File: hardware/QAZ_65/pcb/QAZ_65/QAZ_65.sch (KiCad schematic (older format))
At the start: 97 parts, among them SW1 PTS525, U1 AP2112K-3.3, U2 STM32F042C6Tx, U3 LP5009RUKR, Y1 8.0000MHz

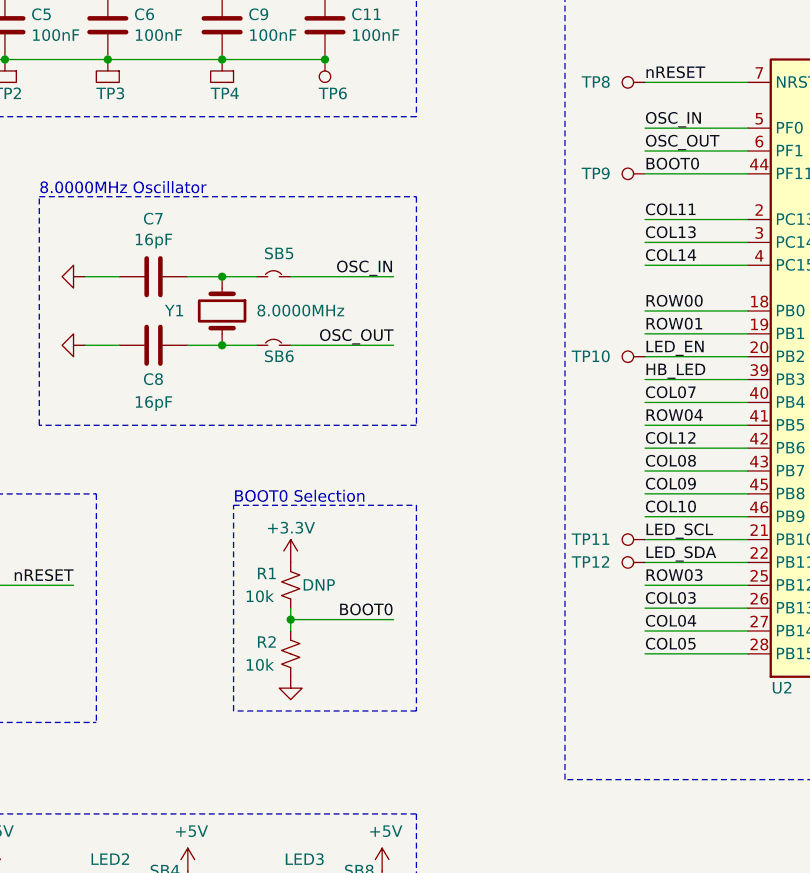
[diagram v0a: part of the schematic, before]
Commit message: qaz v1.1: fixes going from v1.0->v1.1
Changed from individual pull up/down on BOOT0 MCU pin to switch that can
easily change from one to the other (without soldering). This is
required for programming over USB DFU.

Fixed RESET switch, pins were flipped on part layout.
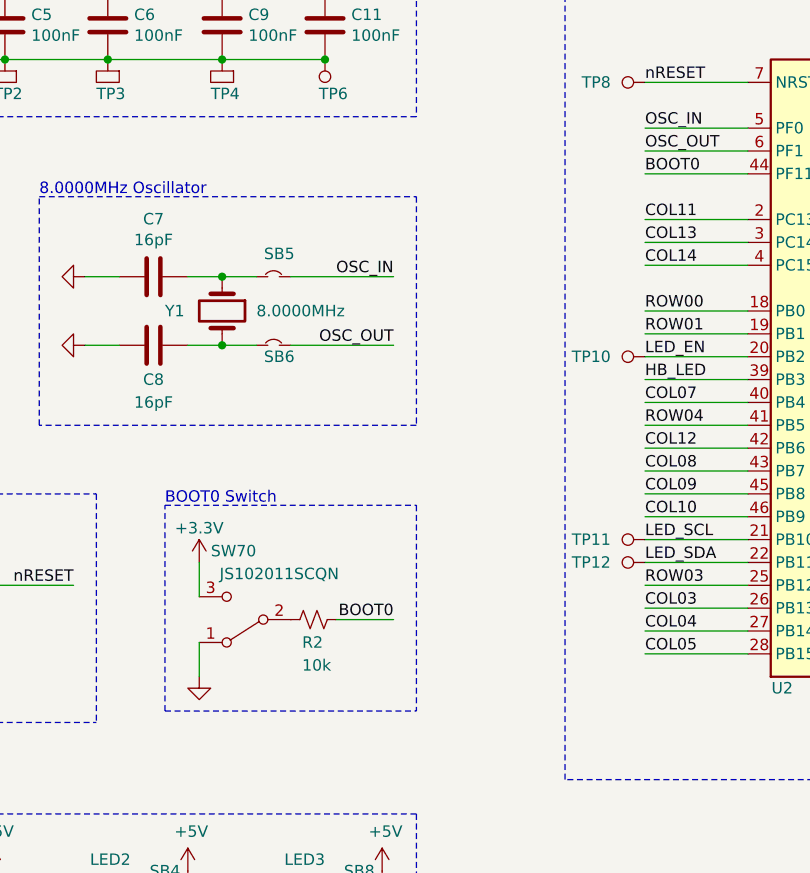
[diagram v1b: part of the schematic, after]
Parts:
- removed R1: 10k, Resistor_SMD:R_0603_1608Metric_Pad1.05x0.95mm_HandSolder, symbol Device:R_Small_US
- removed TP9: TestPoint, QAZ:TestPoint_Thruhole_1.0mm, symbol QAZ:TestPoint_Thruhole_0.7mm
- added SW70: JS102011SCQN, QAZ:JS102011SCQN_SPDT, symbol Switch:SW_SPDT
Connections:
- net +3V3: now also SW70.3 (C)
- net GND: now also SW70.1 (A); no longer R2.1
- new net: R2.1, SW70.2 (B)
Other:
- note added: "BOOT0 Switch"
- note removed: "BOOT0 Selection"
- moved on the sheet: R2
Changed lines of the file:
@@
 EESchema Schematic File Version 4
+LIBS:QAZ_65-cache
 EELAYER 30 0
 EELAYER END
@@
 Sheet 1 3
 Title "QAZ 65% Main"
-Date "2020-11-04"
-Rev "v1.0"
+Date "2020-12-23"
+Rev "v1.1"
 Comp "Anthony Needles"
 Comment1 ""
@@
 Connection ~ 1250 4200
 $Comp
-L Device:R_Small_US R1
-U 1 1 5E2DED31
-P 3350 3950
-F 0 "R1" H 3500 3900 50  0000 R CNN
-F 1 "10k" H 3550 4000 50  0000 R CNN
-F 2 "Resistor_SMD:R_0603_1608Metric_Pad1.05x0.95mm_HandSolder" H 3350 3950 50  0001 C CNN
-F 3 "~" H 3350 3950 50  0001 C CNN
-F 4 "DNP" H 3300 3950 50  0000 R CNN "Comment"
-	1    3350 3950
-	-1   0    0    1
-$EndComp
-$Comp
 L Device:R_Small_US R2
 U 1 1 5E2DEDBB
-P 3350 4250
-F 0 "R2" H 3500 4200 50  0000 R CNN
-F 1 "10k" H 3550 4300 50  0000 R CNN
-F 2 "Resistor_SMD:R_0603_1608Metric_Pad1.05x0.95mm_HandSolder" H 3350 4250 50  0001 C CNN
-F 3 "~" H 3350 4250 50  0001 C CNN
-	1    3350 4250
-	-1   0    0    1
+P 3450 4100
+F 0 "R2" V 3350 4150 50  0000 R CNN
+F 1 "10k" V 3250 4150 50  0000 R CNN
+F 2 "Resistor_SMD:R_0603_1608Metric_Pad1.05x0.95mm_HandSolder" H 3450 4100 50  0001 C CNN
+F 3 "~" H 3450 4100 50  0001 C CNN
+	1    3450 4100
+	0    -1   -1   0
 $EndComp
 $Comp
 L power:GND #PWR014
 U 1 1 5E2DF23D
-P 3350 4350
-F 0 "#PWR014" H 3350 4100 50  0001 C CNN
-F 1 "GND" H 3355 4177 50  0001 C CNN
-F 2 "" H 3350 4350 50  0001 C CNN
-F 3 "" H 3350 4350 50  0001 C CNN
-	1    3350 4350
+P 2950 4350
+F 0 "#PWR014" H 2950 4100 50  0001 C CNN
+F 1 "GND" H 2955 4177 50  0001 C CNN
+F 2 "" H 2950 4350 50  0001 C CNN
+F 3 "" H 2950 4350 50  0001 C CNN
+	1    2950 4350
 	1    0    0    -1
 $EndComp
@@
 L power:+3.3V #PWR013
 U 1 1 5E2DF2F4
-P 3350 3850
-F 0 "#PWR013" H 3350 3700 50  0001 C CNN
-F 1 "+3.3V" H 3350 4000 50  0000 C CNN
-F 2 "" H 3350 3850 50  0001 C CNN
-F 3 "" H 3350 3850 50  0001 C CNN
-	1    3350 3850
-	1    0    0    -1
-$EndComp
-Wire Wire Line
-	3350 4100 3350 4150
-Wire Wire Line
-	3350 4100 3350 4050
-Connection ~ 3350 4100
+P 2950 3850
+F 0 "#PWR013" H 2950 3700 50  0001 C CNN
+F 1 "+3.3V" H 2950 4000 50  0000 C CNN
+F 2 "" H 2950 3850 50  0001 C CNN
+F 3 "" H 2950 3850 50  0001 C CNN
+	1    2950 3850
+	1    0    0    -1
+$EndComp
 $Comp
 L Regulator_Linear:AP2112K-3.3 U1
@@
 Text Notes 2250 2250 0    50   ~ 0
 8.0000MHz Oscillator
-Wire Wire Line
-	3350 4100 3800 4100
 Text Label 3800 4100 2    50   ~ 0
 BOOT0
 Wire Notes Line
-	3100 3600 3900 3600
-Wire Notes Line
 	3900 3600 3900 4500
 Wire Notes Line
-	3900 4500 3100 4500
-Wire Notes Line
-	3100 4500 3100 3600
-Text Notes 3100 3600 0    50   ~ 0
-BOOT0 Selection
+	2800 4500 2800 3600
+Text Notes 2800 3600 0    50   ~ 0
+BOOT0 Switch
 Text Notes 4550 1100 0    50   ~ 0
 MCU
@@
 Text Label 8200 5900 0    50   ~ 0
 USB_D-
-$Comp
-L QAZ:TestPoint_Thruhole_0.7mm TP9
-U 1 1 5F9FCEFD
-P 4900 2150
-F 0 "TP9" V 4900 2300 50  0000 L CNN
-F 1 "TestPoint" H 4900 2000 50  0001 C CNN
-F 2 "QAZ:TestPoint_Thruhole_1.0mm" H 4900 2150 50  0001 C CNN
-F 3 "" H 4900 2150 50  0001 C CNN
-	1    4900 2150
-	0    -1   -1   0
-$EndComp
 Connection ~ 1700 6650
 Wire Wire Line
@@
 NoConn ~ 6550 3150
 NoConn ~ 6550 2750
+$Comp
+L Switch:SW_SPDT SW70
+U 1 1 5FE5583C
+P 3150 4100
+F 0 "SW70" H 3200 3800 50  0000 C CNN
+F 1 "JS102011SCQN" H 3000 3900 50  0000 C CNN
+F 2 "QAZ:JS102011SCQN_SPDT" H 3150 4100 50  0001 C CNN
+F 3 "~" H 3150 4100 50  0001 C CNN
+	1    3150 4100
+	-1   0    0    1
+$EndComp
+Wire Wire Line
+	3550 4100 3800 4100
+Wire Wire Line
+	2950 4350 2950 4200
+Wire Wire Line
+	2950 4000 2950 3850
+Wire Notes Line
+	2800 4500 3900 4500
+Wire Notes Line
+	2800 3600 3900 3600
 $EndSCHEMATC

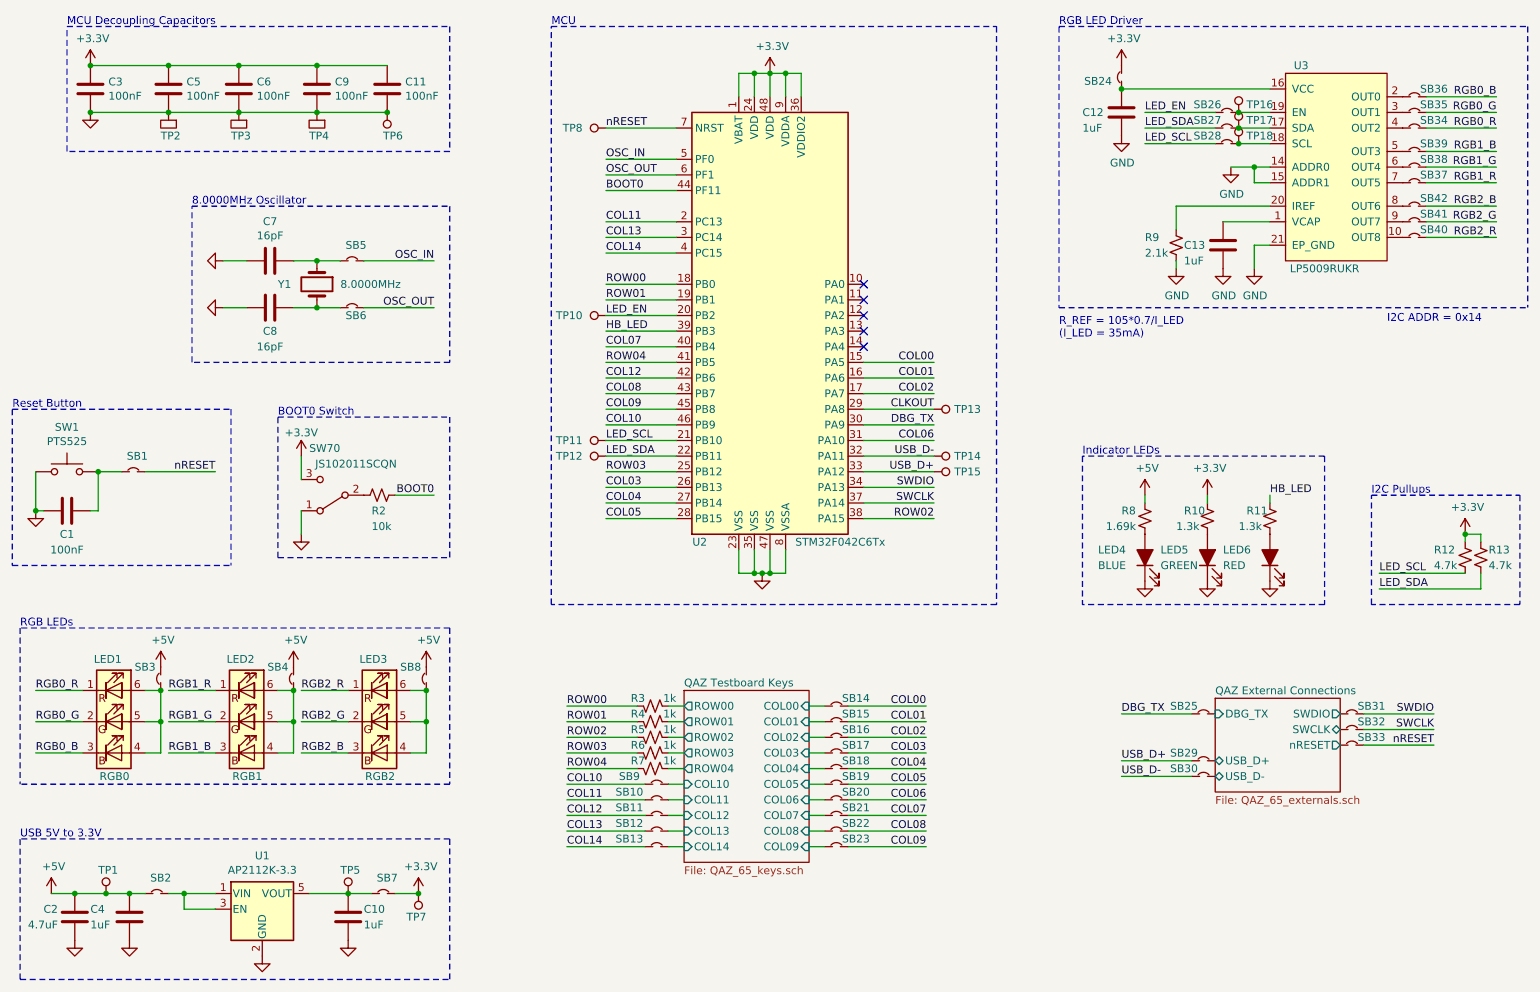
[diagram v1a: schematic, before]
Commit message: QAZ 65% v1.1: updating from v1.0
closes #5
closes #3

QAZ 65% v1.1:

 - Switch for BOOT (PG for booting into bootloader tor ProGram the
   board, KB for booting into KeyBoard)
 - New RGB driver IC, which allows driving RGB LEDS in a grid format
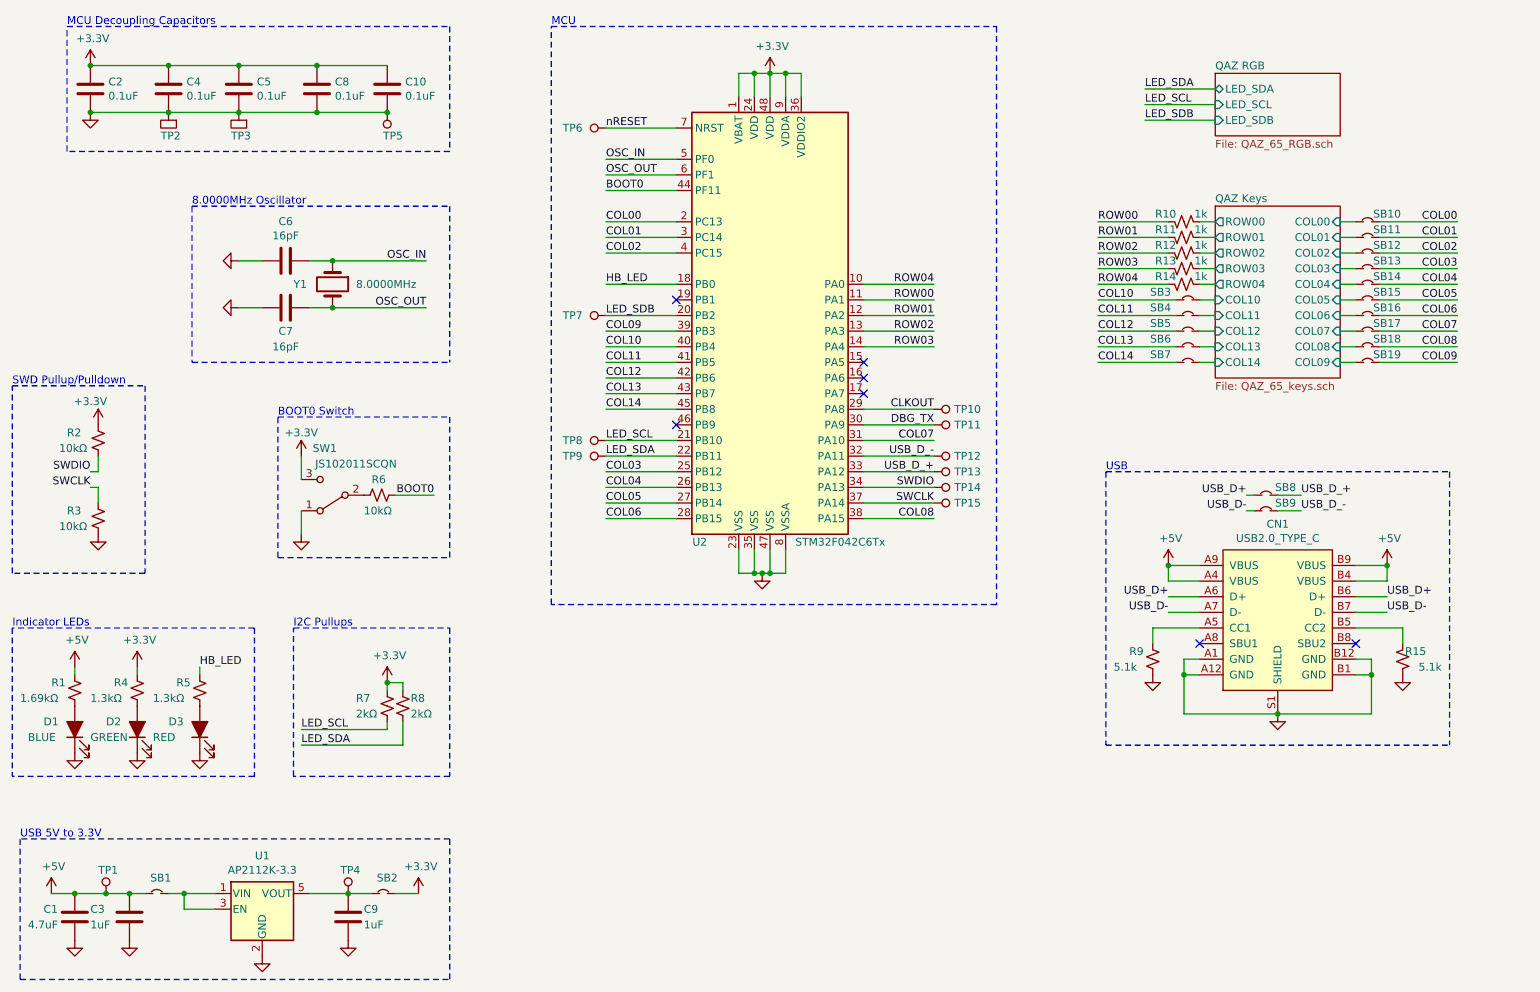
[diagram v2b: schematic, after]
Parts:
- removed C1: 100nF, Capacitor_SMD:C_0603_1608Metric_Pad1.05x0.95mm_HandSolder, symbol Device:C
- removed C12, C13: 1uF, Capacitor_SMD:C_0603_1608Metric_Pad1.05x0.95mm_HandSolder, symbol Device:C
- removed LED1: RGB0, LED_SMD:LED_RGB_PLCC-6, symbol Device:LED_RGB
- removed LED2: RGB1, LED_SMD:LED_RGB_PLCC-6, symbol Device:LED_RGB
- removed LED3: RGB2, LED_SMD:LED_RGB_PLCC-6, symbol Device:LED_RGB
- removed R12, R13: 4.7k, Resistor_SMD:R_0603_1608Metric_Pad1.05x0.95mm_HandSolder, symbol Device:R_Small_US
- removed SB1, SB24, SB25, SB26, SB27, SB28, SB29, SB3, SB30, SB31, SB32, SB33, SB34, SB35, SB36, SB37, SB38, SB39, SB4, SB40, SB41, SB42, SB5, SB6: SolderBridge, Resistor_SMD:R_0603_1608Metric_Pad1.05x0.95mm_HandSolder, symbol QAZ:SolderBridge
- removed SW1: PTS525, QAZ:PTS525SM15, symbol Switch:SW_Push
- removed TP16, TP17, TP18, TP7: TestPoint, QAZ:TestPoint_Thruhole_1.0mm, symbol QAZ:TestPoint_Thruhole_0.7mm
- removed TP4: TestPoint_SMD_1812, QAZ:TestPoint_SMD_1812_HS, symbol QAZ:TestPoint_SMD_1812
- removed U3: LP5009RUKR, QAZ:QFN-20-1EP_3x3mm_P0.4mm_EP1.65x1.65mm_HS, symbol QAZ:LP5009RUKR
- added CN1: USB2.0_TYPE_C, QAZ:USB_C_GCT_USB4085, symbol QAZ:USB2.0_TYPE_C
- added R15: 5.1k, Resistor_SMD:R_0603_1608Metric_Pad1.05x0.95mm_HandSolder, symbol Device:R_Small_US
- added R2, R3: 10kΩ, Resistor_SMD:R_0603_1608Metric_Pad1.05x0.95mm_HandSolder, symbol Device:R_Small_US
- added R7, R8: 2kΩ, Resistor_SMD:R_0603_1608Metric_Pad1.05x0.95mm_HandSolder, symbol Device:R_Small_US
- added SB9: SolderBridge, Resistor_SMD:R_0603_1608Metric_Pad1.05x0.95mm_HandSolder, symbol QAZ:SolderBridge
- added TP11, TP14, TP15: TestPoint, QAZ:TestPoint_Thruhole_1.0mm, symbol QAZ:TestPoint_Thruhole_0.7mm
- C10: renamed from C11; value 100nF -> 0.1uF
- C2: renamed from C3; value 100nF -> 0.1uF
- C4: renamed from C5; value 100nF -> 0.1uF
- C5: renamed from C6; value 100nF -> 0.1uF
- C8: renamed from C9; value 100nF -> 0.1uF
- R1: renamed from R8; value 1.69k -> 1.69kΩ
- R4: renamed from R10; value 1.3k -> 1.3kΩ
- R5: renamed from R11; value 1.3k -> 1.3kΩ
- R6: renamed from R2; value 10k -> 10kΩ
- R9: value 2.1k -> 5.1k
- renumbered C2 to C1, C4 to C3, C7 to C6, C8 to C7, C10 to C9, LED4 to D1, LED5 to D2, LED6 to D3, R3 to R10, R4 to R11, R5 to R12, R6 to R13, R7 to R14, SB2 to SB1, SB14 to SB10, SB15 to SB11, SB16 to SB12, SB17 to SB13, SB18 to SB14, SB19 to SB15, SB20 to SB16, SB21 to SB17, SB22 to SB18, SB23 to SB19, SB7 to SB2, SB9 to SB3, SB10 to SB4, SB11 to SB5, SB12 to SB6, SB13 to SB7, SW70 to SW1, TP13 to TP10, TP14 to TP12, TP15 to TP13, TP5 to TP4, TP6 to TP5, TP8 to TP6, TP10 to TP7, TP11 to TP8, TP12 to TP9
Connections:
- net +3V3: now also R2.2, R7.2, R8.2
- net +5V: now also CN1.A4 (VBUS), CN1.A9 (VBUS), CN1.B4 (VBUS), CN1.B9 (VBUS); no longer SB8.2
- net COL00: now also U2.2 (PC13); no longer U2.15 (PA5)
- net COL01: now also U2.3 (PC14); no longer U2.16 (PA6)
- net COL02: now also U2.4 (PC15); no longer U2.17 (PA7)
- net COL03: now also U2.25 (PB12); no longer U2.26 (PB13)
- net COL04: now also U2.26 (PB13); no longer U2.27 (PB14)
- net COL05: now also U2.27 (PB14); no longer U2.28 (PB15)
- net COL06: now also U2.28 (PB15); no longer U2.31 (PA10)
- net COL07: now also U2.31 (PA10); no longer U2.40 (PB4)
- net COL08: now also U2.38 (PA15); no longer U2.43 (PB7)
- net COL09: now also U2.39 (PB3); no longer U2.45 (PB8)
- net COL10: now also U2.40 (PB4); no longer U2.46 (PB9)
- net COL11: now also U2.41 (PB5); no longer U2.2 (PC13)
- net COL13: now also U2.43 (PB7); no longer U2.3 (PC14)
- net COL14: now also U2.45 (PB8); no longer U2.4 (PC15)
- net DBG_TX: now also TP11.1 (TP)
- net GND: now also CN1.A1 (GND), CN1.A12 (GND), CN1.B1 (GND), CN1.B12 (GND), CN1.S1 (SHIELD), R15.1, R3.1
- net HB_LED: now also U2.18 (PB0); no longer U2.39 (PB3)
- net LED_SCL: now also R7.1
- net LED_SDA: now also R8.1
- net OSC_IN: now also C6.1, Y1.1
- net OSC_OUT: now also C7.1, Y1.2
- net ROW00: now also U2.11 (PA1); no longer U2.18 (PB0)
- net ROW01: now also U2.12 (PA2); no longer U2.19 (PB1)
- net ROW02: now also U2.13 (PA3); no longer U2.38 (PA15)
- net ROW03: now also U2.14 (PA4); no longer U2.25 (PB12)
- net ROW04: now also U2.10 (PA0); no longer U2.41 (PB5)
- net SWCLK: now also R3.2, TP15.1 (TP)
- net SWDIO: now also R2.1, TP14.1 (TP)
- net USB_D+: now also SB8.1, CN1.A6 (D+), CN1.B6 (D+); no longer TP13.1 (TP), U2.33 (PA12)
- net USB_D-: now also CN1.A7 (D-), CN1.B7 (D-), SB9.1; no longer TP12.1 (TP), U2.32 (PA11)
- net at R9.2: now also CN1.A5 (CC1)
- net LED_EN renamed LED_SDB
- net QAZ Testboard Keys/COL00 renamed QAZ Keys/COL00
- net QAZ Testboard Keys/COL01 renamed QAZ Keys/COL01
- net QAZ Testboard Keys/COL02 renamed QAZ Keys/COL02
- net QAZ Testboard Keys/COL03 renamed QAZ Keys/COL03
- net QAZ Testboard Keys/COL04 renamed QAZ Keys/COL04
- net QAZ Testboard Keys/COL05 renamed QAZ Keys/COL05
- net QAZ Testboard Keys/COL06 renamed QAZ Keys/COL06
- net QAZ Testboard Keys/COL07 renamed QAZ Keys/COL07
- net QAZ Testboard Keys/COL08 renamed QAZ Keys/COL08
- net QAZ Testboard Keys/COL09 renamed QAZ Keys/COL09
- net QAZ Testboard Keys/COL10 renamed QAZ Keys/COL10
- net QAZ Testboard Keys/COL11 renamed QAZ Keys/COL11
- net QAZ Testboard Keys/COL12 renamed QAZ Keys/COL12
- net QAZ Testboard Keys/COL13 renamed QAZ Keys/COL13
- net QAZ Testboard Keys/COL14 renamed QAZ Keys/COL14
- net QAZ Testboard Keys/ROW00 renamed QAZ Keys/ROW00
- net QAZ Testboard Keys/ROW01 renamed QAZ Keys/ROW01
- net QAZ Testboard Keys/ROW02 renamed QAZ Keys/ROW02
- net QAZ Testboard Keys/ROW03 renamed QAZ Keys/ROW03
- net QAZ Testboard Keys/ROW04 renamed QAZ Keys/ROW04
- new net: CN1.B5 (CC2), R15.2
- new net USB_D_+: SB8.2, TP13.1 (TP), U2.33 (PA12)
- new net USB_D_-: SB9.2, TP12.1 (TP), U2.32 (PA11)
- no-connect marks 5 -> 7
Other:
- note added: "I2C Pullups\n"
- note added: "SWD Pullup/Pulldown"
- note added: "USB"
- note removed: "I2C ADDR = 0x14"
- note removed: "I2C Pullups"
- note removed: "RGB LED Driver"
- note removed: "RGB LEDs"
- note removed: "R_REF = 105*0.7/I_LED\n(I_LED = 35mA)"
- note removed: "Reset Button"
- moved on the sheet: C6, C7, D1, D2, D3, R1, R10, R11, R12, R13, R14, R4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

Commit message: breakout: rgb conversion board
Made a conversion board for the LED driver conversion board. The RGB
LEDs chosen will not fit, and must be replaced in QAZ v1.1.
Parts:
- added H1, H2, H3, H4, H5, H6: MountingHole, QAZ:4-40_NPTH, symbol Mechanical:MountingHole
- added JP1, JP2, JP3: Jumper_NC_Small, Connector_PinHeader_1.27mm:PinHeader_1x02_P1.27mm_Vertical, symbol Device:Jumper_NC_Small
- R10, R11, R12, R13, R14: value 1k -> 1kΩ
- R15, R9: value 5.1k -> 5.1kΩ
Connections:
- net +3V3: now also JP2.1; no longer R4.2
- net +5V: now also JP1.1; no longer R1.2
- net HB_LED: now also JP3.1; no longer R5.2
- new net: JP1.2, R1.2
- new net: JP2.2, R4.2
- new net: JP3.2, R5.2
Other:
- note added: "Mounting Holes"
- moved on the sheet: C10, C2, C4, C5, C6, C7, C8, R2, R3, R6, SW1, TP2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
